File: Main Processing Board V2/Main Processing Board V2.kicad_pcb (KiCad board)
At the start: 2 copper layers, 37.3 x 37.8 mm, 22 parts, among them J1 Conn_01x10_MountingPin, J4 Conn_01x06_MountingPin, U2 LSM6DSOXTR, U3 Seeed Studio RA4M1, U4 MS5611-01BA03, U5 MMC5603NJ

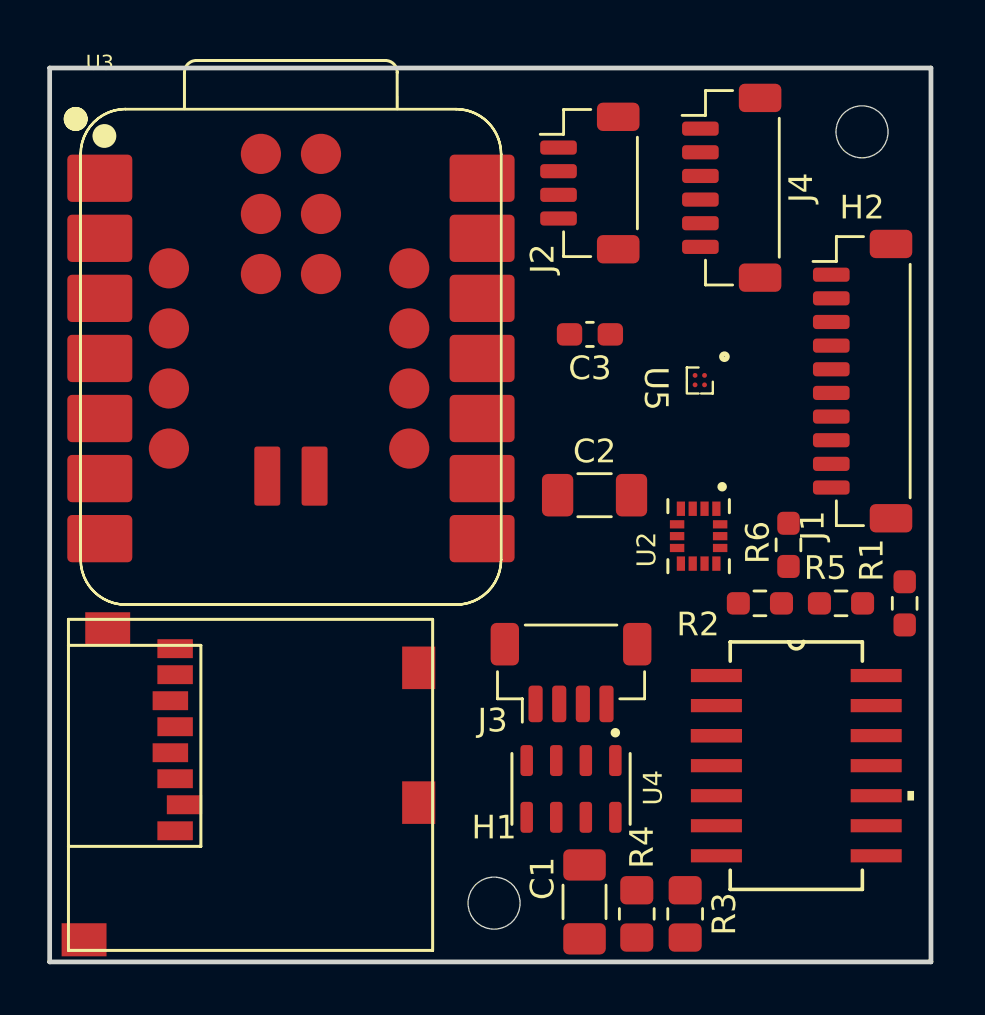
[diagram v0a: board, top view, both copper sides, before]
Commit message: started routing
added ground plane
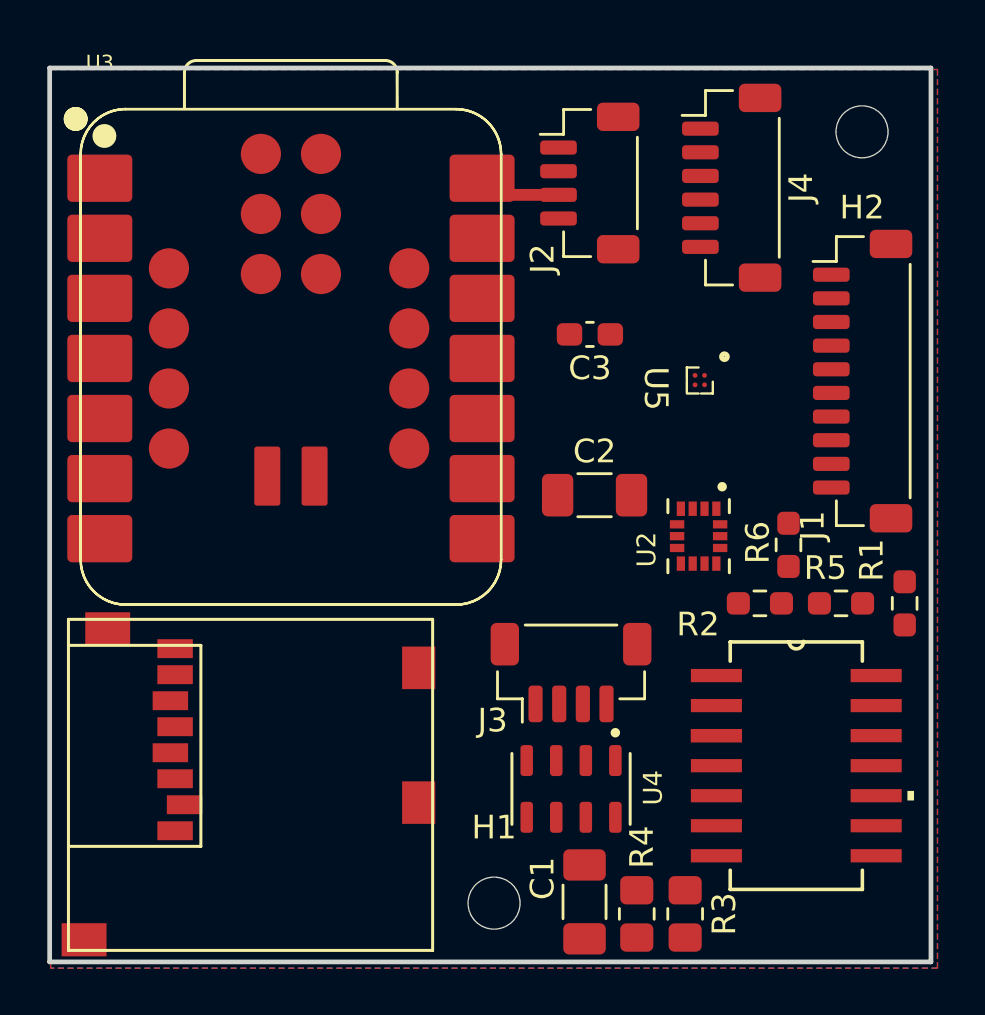
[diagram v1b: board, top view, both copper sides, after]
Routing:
- net +5V: track 0.00 -> 3.52 mm
- added copper zone on B.Cu, net GND
- added copper zone on F.Cu, net GND
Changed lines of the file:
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@@
 		(layer "Edge.Cuts")
+	)
+	(segment
+		(start 151.945738 76.3)
+		(end 151.2432 75.597462)
+		(width 0.2)
+		(layer "F.Cu")
+		(net 6)
+	)
+	(segment
+		(start 154.475 76.3)
+		(end 151.945738 76.3)
+		(width 0.5)
+		(layer "F.Cu")
+		(net 6)
 	)
 	(zone
@@
 			)
 		)
+	)
+	(zone
+		(net 7)
+		(net_name "GND")
+		(layers "F.Cu" "B.Cu")
+		(hatch edge 0.5)
+		(connect_pads
+			(clearance 0.5)
+		)
+		(min_thickness 0.25)
+		(filled_areas_thickness no)
+		(fill
+			(thermal_gap 0.5)
+			(thermal_bridge_width 0.5)
+		)
+		(polygon
+			(pts
+				(xy 133 71) (xy 170.5 71) (xy 170.5 109) (xy 133 109)
+			)
+		)

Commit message: more routing
I worked on the routing some more, focusing mostly on the bottom right corner. I still need to change the thickness of the connections I made to 0.5
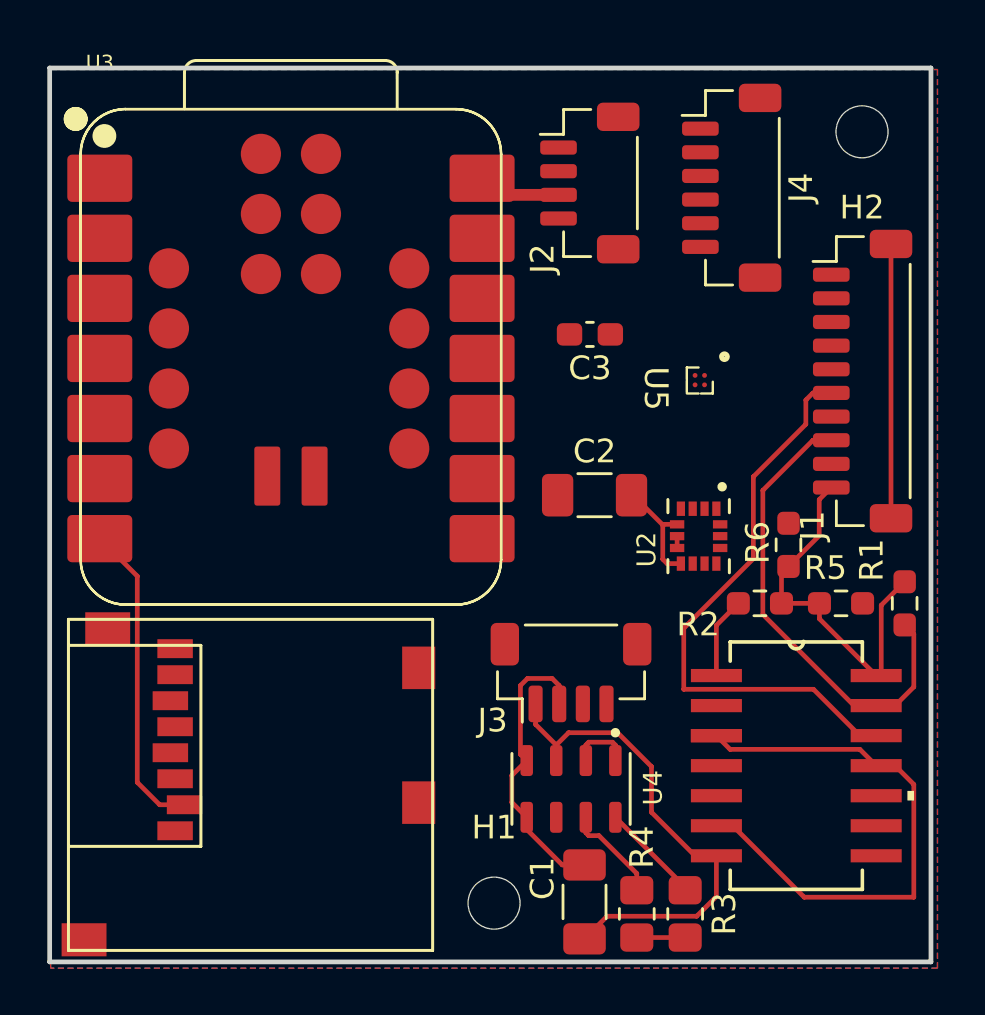
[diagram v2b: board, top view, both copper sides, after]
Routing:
- net +3.3V: track 0.00 -> 38.8 mm
- net /MISO: track 0.00 -> 25.2 mm
- net /Radio_MISO: track 0.00 -> 24.5 mm
- net GND: track 0.00 -> 21.6 mm
- net /Radio_CS: track 0.00 -> 20.1 mm
- net /SD_CS: track 0.00 -> 16.8 mm
- net unconnected-(J1-MountPin-PadMP): track 0.00 -> 11.6 mm
- net /SCL_I2C: track 0.00 -> 4.31 mm
- net /SDA_I2C: track 0.00 -> 4.23 mm
- net /CAMERA_CS: track 0.00 -> 0.80 mm

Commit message: more routing
I did some more routing. Will likely have to redo part of it, as I'm getting stuck
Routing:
- net +3.3V: track 38.8 -> 109.1 mm, vias 0 -> 6
- net /MOSI: track 0.00 -> 63.6 mm, vias 0 -> 4
- net /SCL_I2C: track 4.31 -> 59.4 mm, vias 0 -> 2
- net GND: track 21.6 -> 75.0 mm, vias 0 -> 2
- net /SCK_SPI: track 0.00 -> 52.6 mm, vias 0 -> 4
- net /CAMERA_CS: track 0.80 -> 50.5 mm, vias 0 -> 5
- net /Radio_Reset: track 0.00 -> 45.3 mm, vias 0 -> 2
- net /Radio_EN: track 0.00 -> 39.3 mm, vias 0 -> 2
- net /Camera_MISO: track 0.00 -> 36.1 mm, vias 0 -> 2
- net /SDA_I2C: track 4.23 -> 34.3 mm
- net /SD_CS: track 16.8 -> 46.0 mm, vias 0 -> 2
- net /SD_MISO: track 0.00 -> 29.0 mm, vias 0 -> 2
- net +5V: track 3.52 -> 17.1 mm, vias 0 -> 2

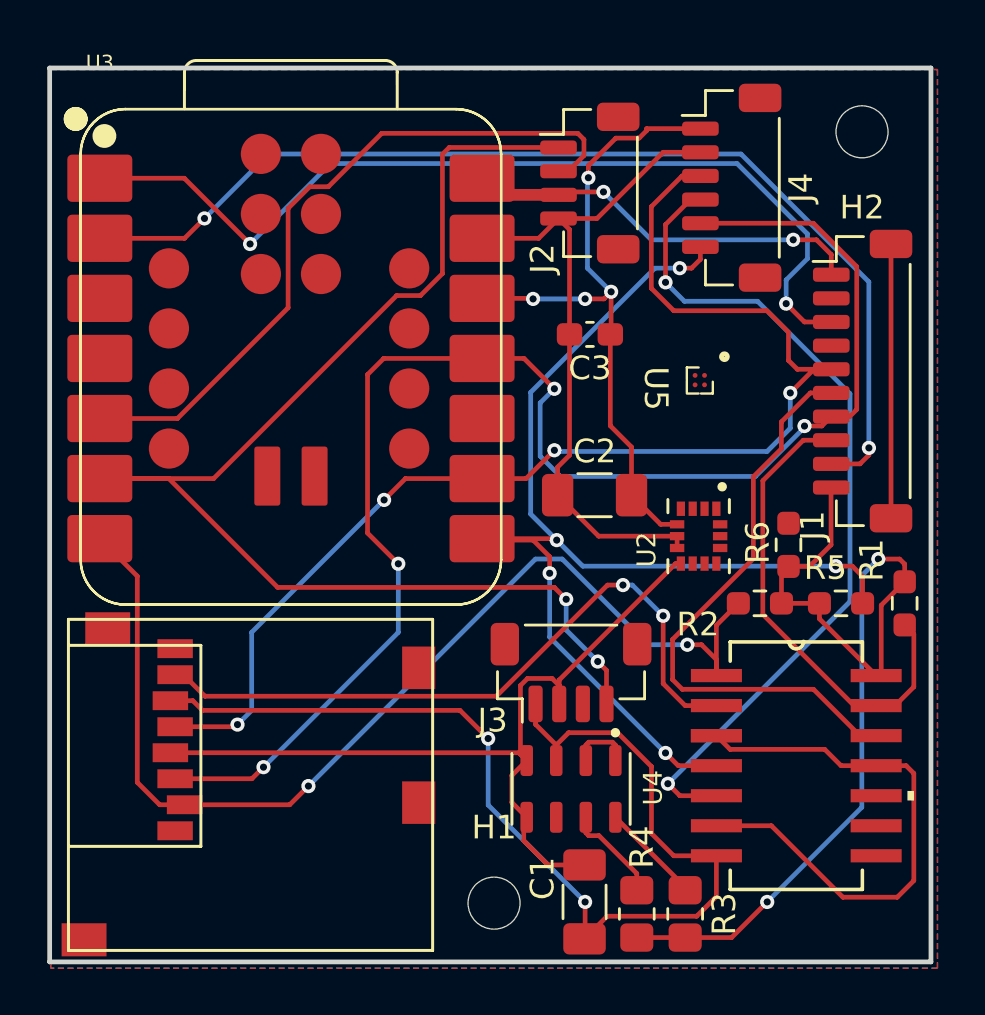
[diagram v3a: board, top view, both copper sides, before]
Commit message: more routing
Did as much as I could but got stuck so will need to redo some parts.
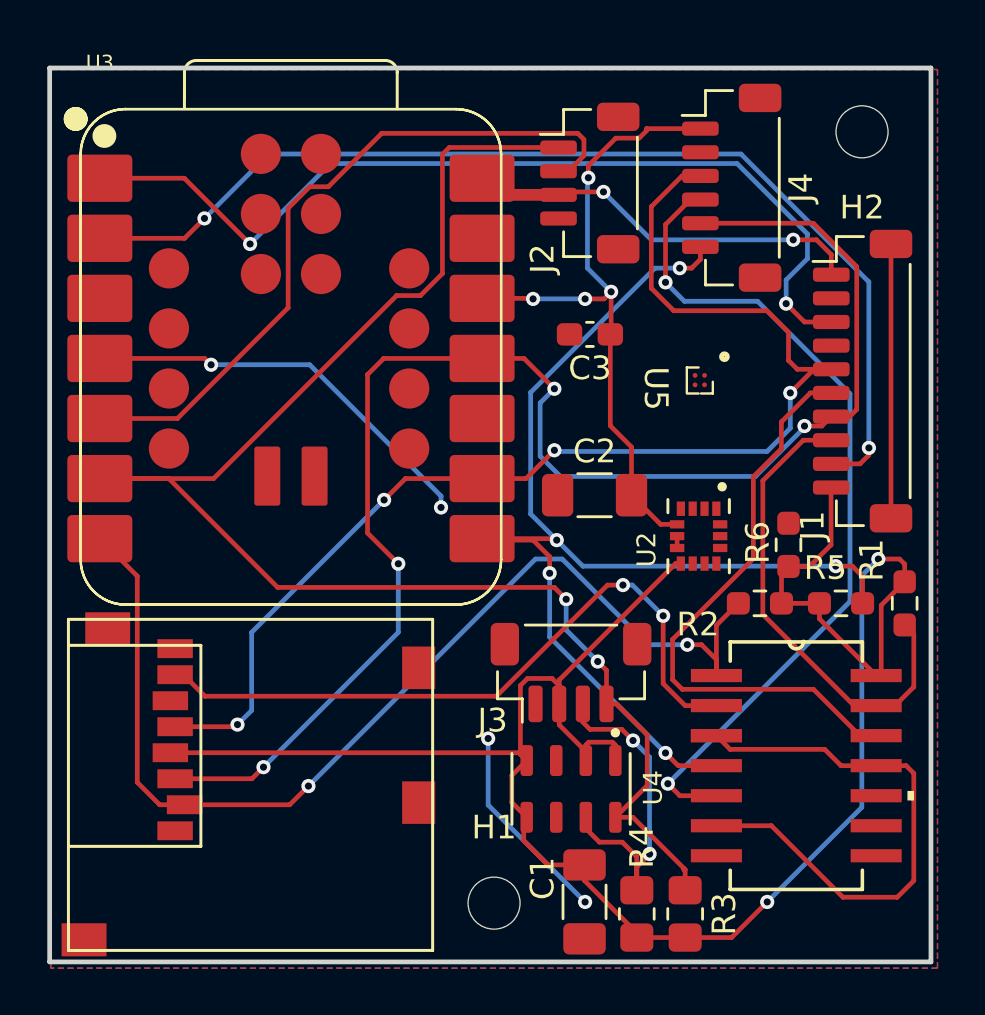
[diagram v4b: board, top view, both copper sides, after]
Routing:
- net GND: track 75.0 -> 9.14 mm
- net /Radio_CS: track 20.3 -> 37.7 mm, vias 0 -> 2
- net /SDA_I2C: track 34.3 -> 44.7 mm, vias 0 -> 2
- net +3.3V: track 109.1 -> 115.9 mm
- net /SCL_I2C: track 59.4 -> 66.2 mm

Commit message: Finished PCB Routing
There were some merge conflicts, so if something seems off, then it probably is.
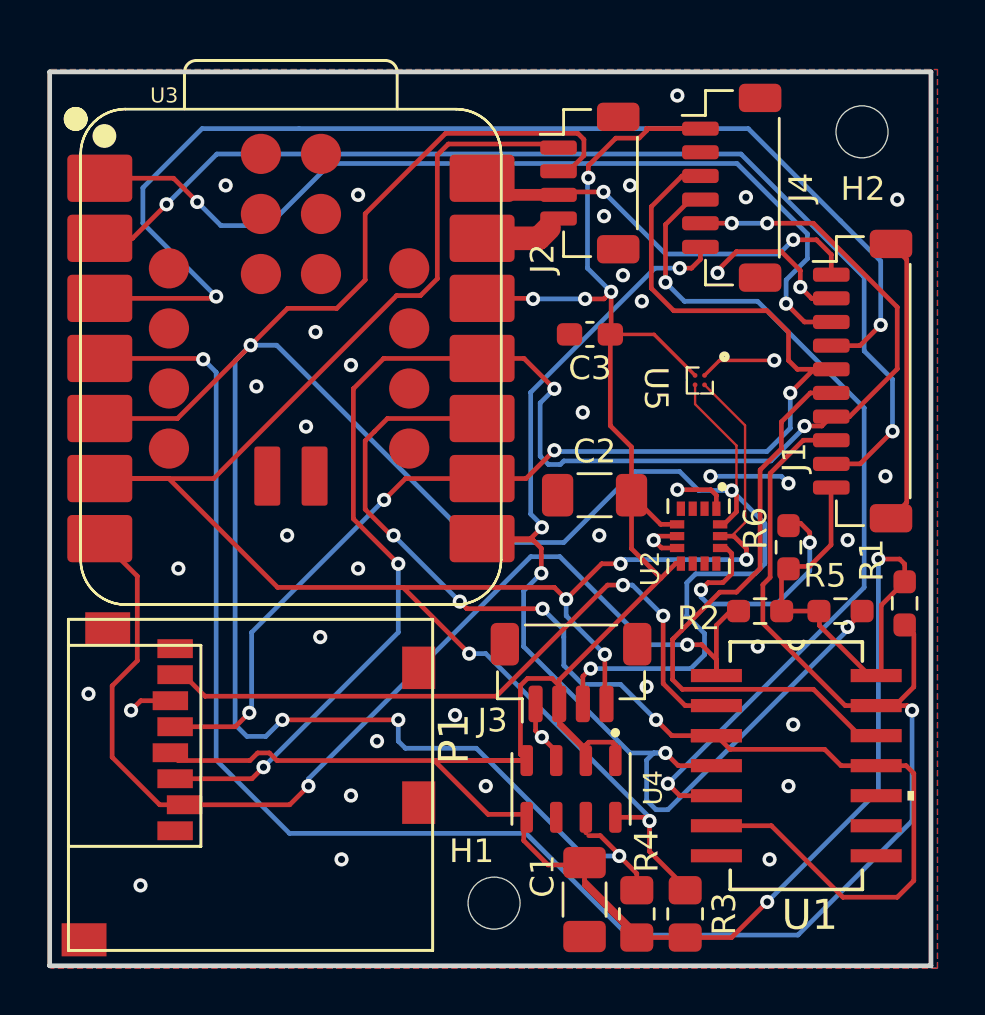
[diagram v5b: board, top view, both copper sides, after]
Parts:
- moved R5 0.33 mm to (166.4, 93.9)
- moved R2 0.33 mm to (163.0, 93.9)
- moved R6 0.10 mm to (164.2, 91.2)
- moved C1 0.10 mm to (155.6, 106.1)
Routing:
- net /SDA_I2C: track 44.7 -> 120.1 mm, vias 2 -> 6
- net /Radio_G0: track 0.00 -> 50.5 mm, vias 0 -> 2
- net /Radio_CS: track 37.7 -> 82.9 mm
- net /MISO: track 25.0 -> 53.0 mm, vias 0 -> 4
- net /SCL_I2C: track 66.2 -> 93.1 mm, vias 2 -> 6
- net +3.3V: track 115.9 -> 135.5 mm
- net GND: track 9.14 -> 25.3 mm, vias 2 -> 42
- net Net-(U2-CS): track 0.00 -> 11.3 mm, vias 0 -> 2
- net /MOSI: track 63.6 -> 65.1 mm, vias 4 -> 6
- net /CAMERA_CS: track 50.5 -> 51.9 mm
- net /SD_CS: track 46.0 -> 47.2 mm
- net /Radio_Reset: track 45.3 -> 46.1 mm
- net /Radio_EN: track 39.3 -> 38.6 mm
- net unconnected-(J1-MountPin-PadMP): track 11.6 -> 12.2 mm
